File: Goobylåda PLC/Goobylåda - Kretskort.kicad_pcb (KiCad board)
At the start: 2 copper layers, 100 x 100 mm, 99 parts, among them J1 LCD 1602 kontakt, J10 Anslutning, J11 Anslutning, J12 Anslutning, J13 Anslutning, J14 Anslutning, J15 Anslutning, J16 Anslutning, J17 Anslutning, J18 Anslutning, J2 Anslutning, J3 Anslutning, J4 Anslutning, J5 Anslutning, J6 Anslutning, J7 Anslutning, J8 Anslutning, J9 Anslutning, Q1 2N2222, Q10 MJE29555T, Q11 MJE29555T, Q12 MJE29555T, Q2 2N2222, Q3 2N2222, Q4 IRF9630, Q5 IRF9630, Q6 IRF9630, Q7 2N2222, Q8 2N2222, Q9 2N2222, U1 LM7812_TO220

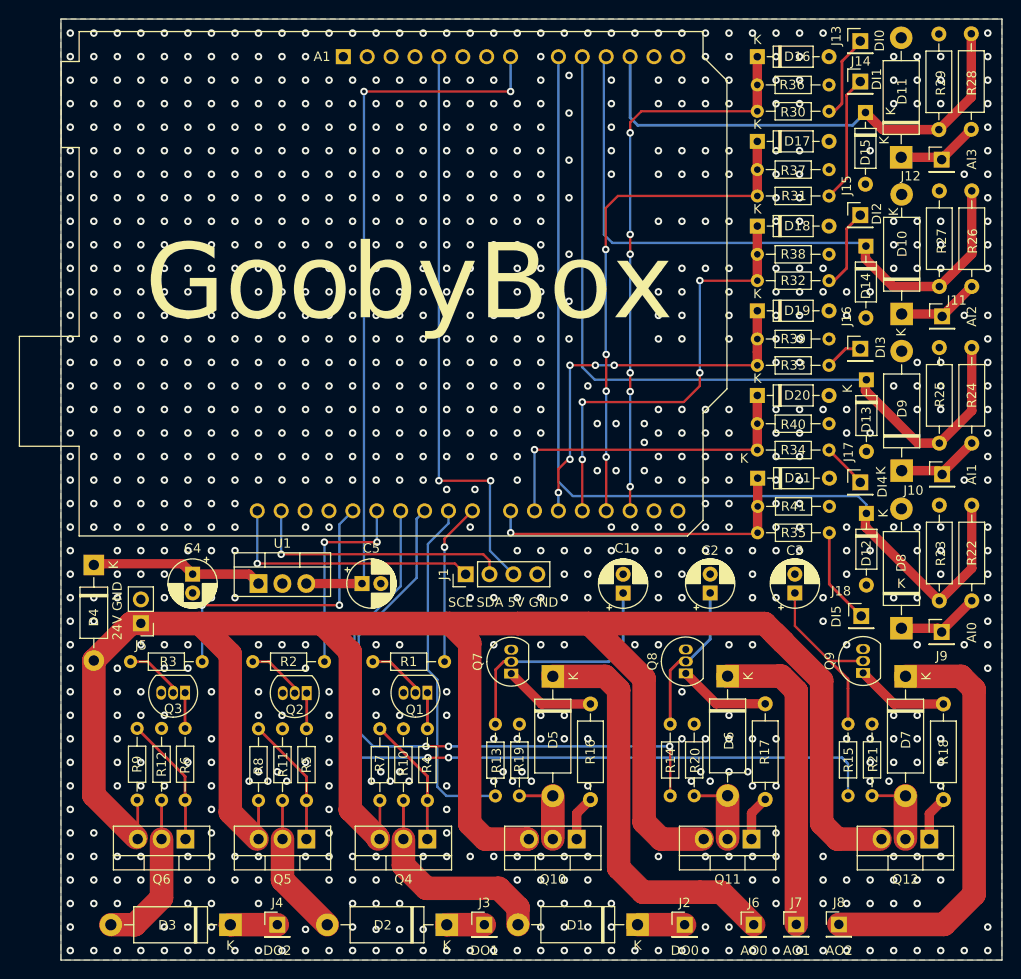
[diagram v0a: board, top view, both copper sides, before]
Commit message: mounting holes
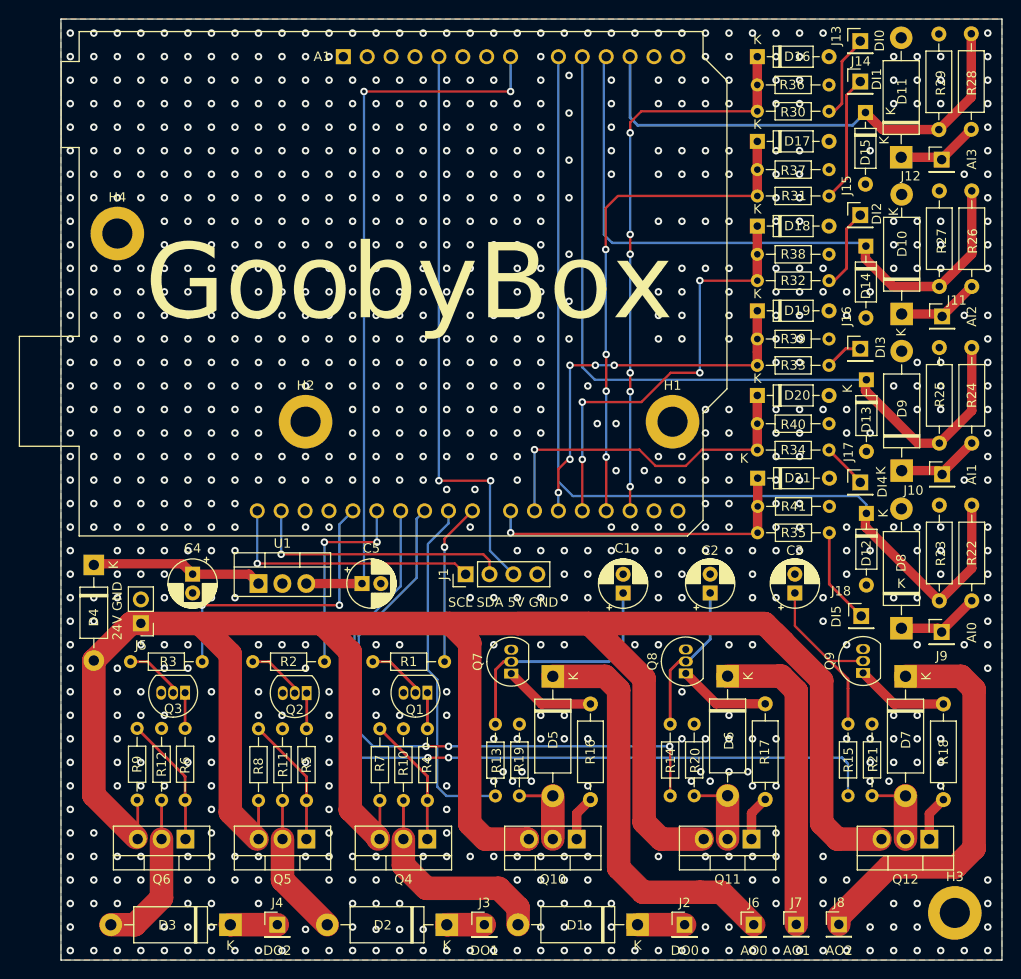
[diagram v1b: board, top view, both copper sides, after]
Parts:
- added H1: M3, MountingHole:MountingHole_3.2mm_M3_ISO7380_Pad, F.Cu at (154.0, 83.8)
- added H2: M3, MountingHole:MountingHole_3.2mm_M3_ISO7380_Pad, F.Cu at (115.0, 83.8)
- added H3: M3, MountingHole:MountingHole_3.2mm_M3_ISO7380_Pad, F.Cu at (184.0, 136.0)
- added H4: M3, MountingHole:MountingHole_3.2mm_M3_ISO7380_Pad, F.Cu at (95.0, 63.8)
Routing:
- net /AO_2: track 45.3 -> 43.0 mm
- net /DI6: track 36.0 -> 37.4 mm
- net /DI4: track 47.9 -> 47.1 mm
- net GND: vias 917 -> 896
- net (no net): vias 11 -> 0
